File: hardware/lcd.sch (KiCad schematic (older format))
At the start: 3 parts, among them J6 LCD Display

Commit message: Hardware Projekt knovertiert von KiCad 4 -> KiCad 5 - Schaltplan angepasst - neues Detailfoto hinzugefügt - Footprints neu zugeordnet, somit ist auch wieder eine 3D Darstellung möglich - Readme.md angepasst
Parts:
- J6: footprint w_conn_strip:vasch_strip_5x2 -> Connector_IDC:IDC-Header_2x05_P2.54mm_Vertical; symbol Conn_02x05_Odd_Even -> Connector_Generic:Conn_02x05_Odd_Even
- R10: footprint Discret:R4-5 -> Resistor_THT:R_Axial_DIN0207_L6.3mm_D2.5mm_P10.16mm_Horizontal; symbol R -> Device:R
- RV1: footprint w_pth_resistors:trimmer_vishay_64w -> Potentiometer_THT:Potentiometer_Bourns_3296W_Vertical; symbol POT-RESCUE-1541-rebuild -> Device:R_POT
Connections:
- net labels added: D4, D5, D6, D7
- net labels removed: D0, D1, D2, D3
- wire segments 14 -> 16
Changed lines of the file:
@@
-EESchema Schematic File Version 2
-LIBS:power
-LIBS:1541-rebuild-rescue
-LIBS:device
-LIBS:transistors
-LIBS:conn
-LIBS:linear
-LIBS:regul
-LIBS:74xx
-LIBS:cmos4000
-LIBS:adc-dac
-LIBS:memory
-LIBS:xilinx
-LIBS:microcontrollers
-LIBS:dsp
-LIBS:microchip
-LIBS:analog_switches
-LIBS:motorola
-LIBS:texas
-LIBS:intel
-LIBS:audio
-LIBS:interface
-LIBS:digital-audio
-LIBS:philips
-LIBS:display
-LIBS:cypress
-LIBS:siliconi
-LIBS:opto
-LIBS:atmel
-LIBS:contrib
-LIBS:valves
-LIBS:Oscillators
-LIBS:w_analog
-LIBS:w_connectors
-LIBS:w_device
-LIBS:w_logic
-LIBS:w_memory
-LIBS:w_microcontrollers
-LIBS:w_opto
-LIBS:w_relay
-LIBS:w_rtx
-LIBS:w_transistor
-LIBS:w_vacuum
-LIBS:ka_sd_sockets
+EESchema Schematic File Version 4
 LIBS:1541-rebuild-cache
-EELAYER 25 0
+EELAYER 30 0
 EELAYER END
 $Descr A4 11693 8268
@@
 Sheet 3 4
 Title "1541-rebuid"
-Date "2018-05-16"
-Rev "1.3.5"
+Date "2020-04-14"
+Rev "1.4.0"
 Comp ""
 Comment1 "Erstellt von: Thorsten Kattanek"
@@
 $EndDescr
 $Comp
-L Conn_02x05_Odd_Even J6
+L Connector_Generic:Conn_02x05_Odd_Even J6
 U 1 1 5AEE2FA0
 P 5050 3600
 F 0 "J6" H 5100 3900 50  0000 C CNN
 F 1 "LCD Display" H 5100 3300 50  0000 C CNN
-F 2 "w_conn_strip:vasch_strip_5x2" H 5050 3600 50  0001 C CNN
+F 2 "Connector_IDC:IDC-Header_2x05_P2.54mm_Vertical" H 5050 3600 50  0001 C CNN
 F 3 "" H 5050 3600 50  0001 C CNN
 	1    5050 3600
@@
 Steckerbelegung für das LCD Display (20x4)\n\nPIN_01: VDD(2) ... +5V\nPIN_02: VSS(1), R/W(5), LED-/K(16) ... GND\nPIN_03: D4(11)\nPIN_04: D5(12)\nPIN_05: D6(13)\nPIN_06: D7(14)\nPIN_07: E(6)\nPIN_08: RS(4)\nPIN_09: LED+/A(15)\nPIN_10: VO(3)\n
 $Comp
-L +5V #PWR020
+L power:+5V #PWR0102
 U 1 1 5AEE3573
 P 5250 2450
-F 0 "#PWR020" H 5250 2300 50  0001 C CNN
+F 0 "#PWR0102" H 5250 2300 50  0001 C CNN
 F 1 "+5V" H 5250 2590 50  0000 C CNN
 F 2 "" H 5250 2450 60  0000 C CNN
@@
 $EndComp
 Text HLabel 5150 2900 1    60   Input ~ 0
-D0
+D4
 Text HLabel 5150 4150 3    60   Input ~ 0
-D1
+D5
 Text HLabel 5050 2900 1    60   Input ~ 0
-D2
+D6
 Text HLabel 5050 4150 3    60   Input ~ 0
-D3
+D7
 Text HLabel 4950 2900 1    60   Input ~ 0
 EN
@@
 RS
 Wire Wire Line
-	5250 2450 5250 3400
+	5250 2450 5250 2550
 Wire Wire Line
 	5150 2900 5150 3400
@@
 	4950 3900 4950 4150
 $Comp
-L R R10
+L Device:R R10
 U 1 1 5AEE40E3
 P 4850 3100
 F 0 "R10" V 4930 3100 50  0000 C CNN
 F 1 "150" V 4850 3100 50  0000 C CNN
-F 2 "Discret:R4-5" V 4780 3100 30  0001 C CNN
+F 2 "Resistor_THT:R_Axial_DIN0207_L6.3mm_D2.5mm_P10.16mm_Horizontal" V 4780 3100 30  0001 C CNN
 F 3 "" H 4850 3100 30  0000 C CNN
 	1    4850 3100
@@
 	4850 3250 4850 3400
 Wire Wire Line
-	5250 3900 5250 4750
+	5250 3900 5250 4550
 $Comp
-L POT-RESCUE-1541-rebuild RV1
+L Device:R_POT RV1
 U 1 1 5AEE481D
 P 4850 4550
-F 0 "RV1" H 4850 4450 50  0000 C CNN
-F 1 "10k" H 4850 4550 50  0000 C CNN
-F 2 "w_pth_resistors:trimmer_vishay_64w" H 4850 4550 60  0001 C CNN
+F 0 "RV1" V 4750 4550 50  0000 C CNN
+F 1 "10k" V 4850 4550 50  0000 C CNN
+F 2 "Potentiometer_THT:Potentiometer_Bourns_3296W_Vertical" H 4850 4550 60  0001 C CNN
 F 3 "" H 4850 4550 60  0000 C CNN
 	1    4850 4550
-	1    0    0    -1
+	0    -1   -1   0
 $EndComp
 Wire Wire Line
-	5100 4550 5250 4550
+	5000 4550 5250 4550
 Connection ~ 5250 4550
 Wire Wire Line
 	4850 3900 4850 4400
 $Comp
-L +5V #PWR021
+L power:+5V #PWR0103
 U 1 1 5AEE4960
 P 4350 4550
-F 0 "#PWR021" H 4350 4400 50  0001 C CNN
+F 0 "#PWR0103" H 4350 4400 50  0001 C CNN
 F 1 "+5V" H 4350 4690 50  0000 C CNN
 F 2 "" H 4350 4550 60  0000 C CNN
@@
 $EndComp
 Wire Wire Line
-	4350 4550 4600 4550
+	4350 4550 4700 4550
 Text Notes 650  7600 0    60   ~ 0
 R10 hängt von der Hintergrundbeleuchtung des LCD Displays ab !
 $Comp
-L GND #PWR022
+L power:GND #PWR0104
 U 1 1 5AF0CC1F
 P 5250 4750
-F 0 "#PWR022" H 5250 4500 50  0001 C CNN
+F 0 "#PWR0104" H 5250 4500 50  0001 C CNN
 F 1 "GND" H 5250 4600 50  0000 C CNN
 F 2 "" H 5250 4750 50  0001 C CNN
@@
 	1    0    0    -1
 $EndComp
+Wire Wire Line
+	5250 2550 5250 3400
+Wire Wire Line
+	5250 4550 5250 4750
 $EndSCHEMATC

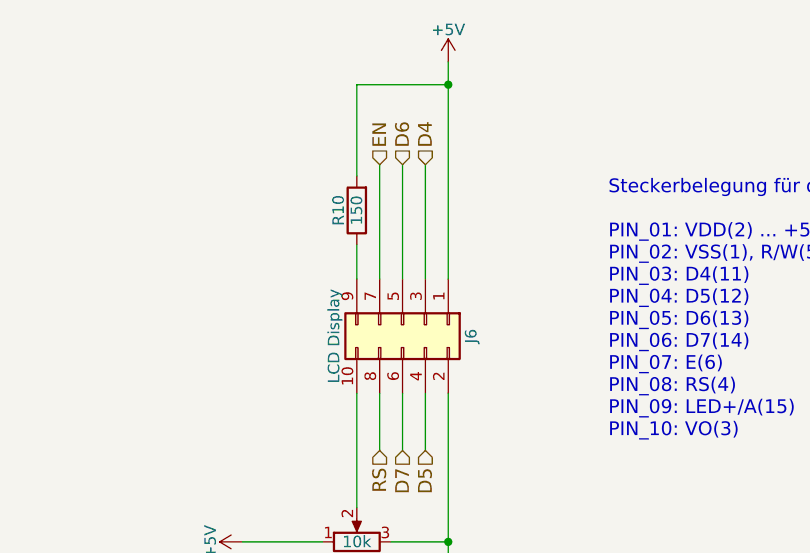
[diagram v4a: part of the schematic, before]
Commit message: Platine geändert - größe angepasst für 1541 I + II - Bauteile neu angeordnet - Beschriftungen hinzugefügt
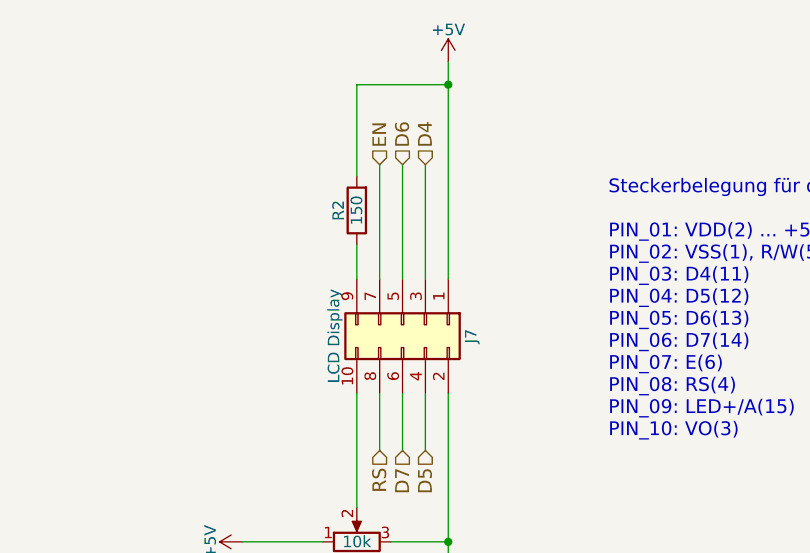
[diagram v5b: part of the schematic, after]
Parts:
- renumbered J6 to J7, R10 to R2
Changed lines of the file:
@@
 $EndDescr
 $Comp
-L Connector_Generic:Conn_02x05_Odd_Even J6
+L Connector_Generic:Conn_02x05_Odd_Even J7
 U 1 1 5AEE2FA0
 P 5050 3600
-F 0 "J6" H 5100 3900 50  0000 C CNN
+F 0 "J7" H 5100 3900 50  0000 C CNN
 F 1 "LCD Display" H 5100 3300 50  0000 C CNN
 F 2 "Connector_IDC:IDC-Header_2x05_P2.54mm_Vertical" H 5050 3600 50  0001 C CNN
@@
 Steckerbelegung für das LCD Display (20x4)\n\nPIN_01: VDD(2) ... +5V\nPIN_02: VSS(1), R/W(5), LED-/K(16) ... GND\nPIN_03: D4(11)\nPIN_04: D5(12)\nPIN_05: D6(13)\nPIN_06: D7(14)\nPIN_07: E(6)\nPIN_08: RS(4)\nPIN_09: LED+/A(15)\nPIN_10: VO(3)\n
 $Comp
-L power:+5V #PWR0102
+L power:+5V #PWR021
 U 1 1 5AEE3573
 P 5250 2450
-F 0 "#PWR0102" H 5250 2300 50  0001 C CNN
+F 0 "#PWR021" H 5250 2300 50  0001 C CNN
 F 1 "+5V" H 5250 2590 50  0000 C CNN
 F 2 "" H 5250 2450 60  0000 C CNN
@@
 	4950 3900 4950 4150
 $Comp
-L Device:R R10
+L Device:R R2
 U 1 1 5AEE40E3
 P 4850 3100
-F 0 "R10" V 4930 3100 50  0000 C CNN
+F 0 "R2" V 4930 3100 50  0000 C CNN
 F 1 "150" V 4850 3100 50  0000 C CNN
 F 2 "Resistor_THT:R_Axial_DIN0207_L6.3mm_D2.5mm_P10.16mm_Horizontal" V 4780 3100 30  0001 C CNN
@@
 	4850 3900 4850 4400
 $Comp
-L power:+5V #PWR0103
+L power:+5V #PWR022
 U 1 1 5AEE4960
 P 4350 4550
-F 0 "#PWR0103" H 4350 4400 50  0001 C CNN
+F 0 "#PWR022" H 4350 4400 50  0001 C CNN
 F 1 "+5V" H 4350 4690 50  0000 C CNN
 F 2 "" H 4350 4550 60  0000 C CNN
@@
 R10 hängt von der Hintergrundbeleuchtung des LCD Displays ab !
 $Comp
-L power:GND #PWR0104
+L power:GND #PWR023
 U 1 1 5AF0CC1F
 P 5250 4750
-F 0 "#PWR0104" H 5250 4500 50  0001 C CNN
+F 0 "#PWR023" H 5250 4500 50  0001 C CNN
 F 1 "GND" H 5250 4600 50  0000 C CNN
 F 2 "" H 5250 4750 50  0001 C CNN

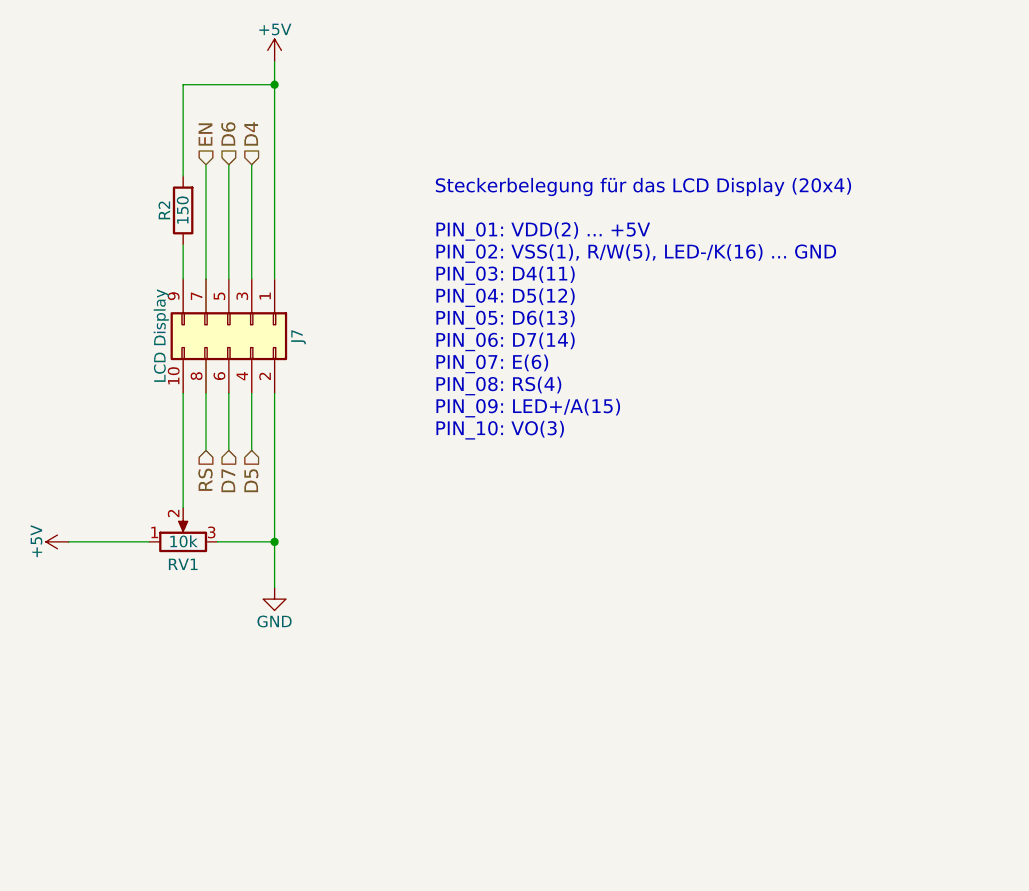
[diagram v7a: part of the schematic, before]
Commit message: major changes for 1.4.1 PCB
created a new PCB for I2C support. all connections rerouted and
a new board needs to be created. layout and footprint taken from 1.4.0
board revision. images from kicad added, README adopted
CAUTION: PCB untested, due to lack of software routines (I2C)
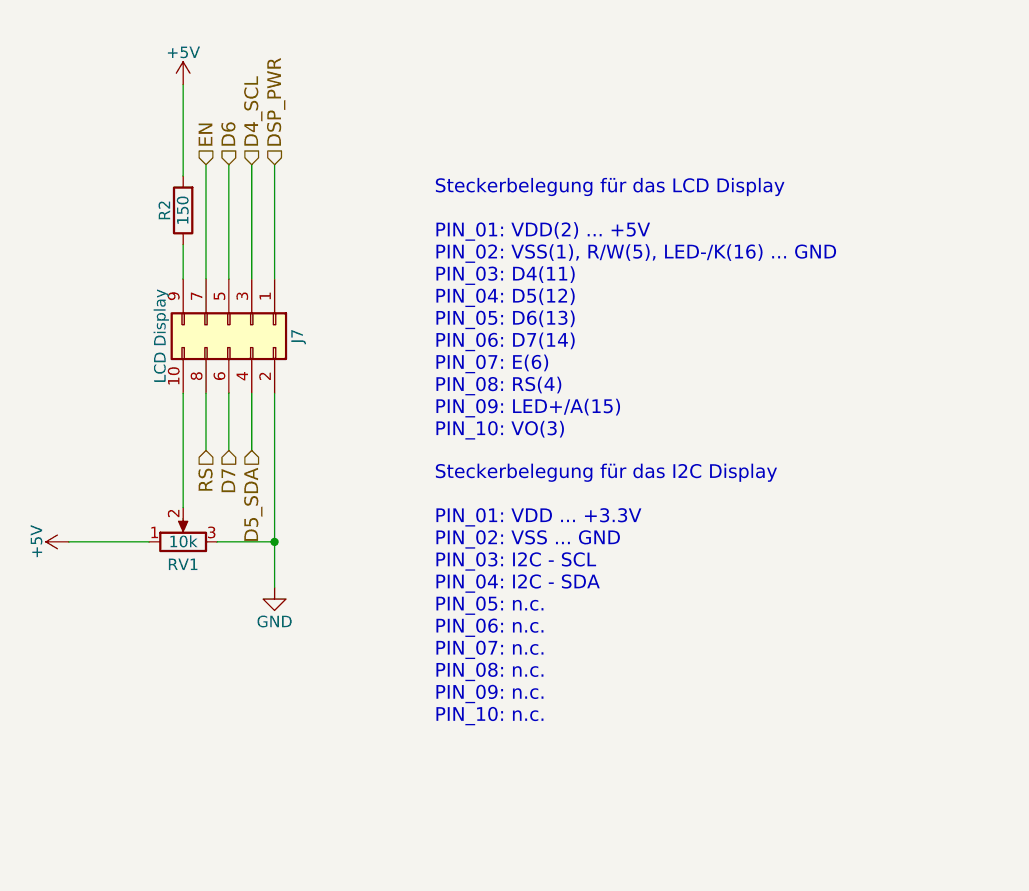
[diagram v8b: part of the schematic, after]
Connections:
- net +5V: no longer J7.1 (Pin_1)
- net D4 renamed D4_SCL
- net D5 renamed D5_SDA
- new net DSP_PWR: J7.1 (Pin_1)
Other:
- note added: "Steckerbelegung für das I2C Display\n\nPIN_01: VDD ... +3.3V\nPIN_02: VSS ... GND\nPIN_03: I2C - SCL\nPIN_04: I2C - SDA\nPIN_05: n.c.\nPIN_06: n.c.\nPIN_07: n.c.\nPIN_08: n.c.\nPIN_09: n.c.\nPIN_10: n.c.\n"
- note added: "Steckerbelegung für das LCD Display\n\nPIN_01: VDD(2) ... +5V\nPIN_02: VSS(1), R/W(5), LED-/K(16) ... GND\nPIN_03: D4(11)\nPIN_04: D5(12)\nPIN_05: D6(13)\nPIN_06: D7(14)\nPIN_07: E(6)\nPIN_08: RS(4)\nPIN_09: LED+/A(15)\nPIN_10: VO(3)\n"
- note removed: "Steckerbelegung für das LCD Display (20x4)\n\nPIN_01: VDD(2) ... +5V\nPIN_02: VSS(1), R/W(5), LED-/K(16) ... GND\nPIN_03: D4(11)\nPIN_04: D5(12)\nPIN_05: D6(13)\nPIN_06: D7(14)\nPIN_07: E(6)\nPIN_08: RS(4)\nPIN_09: LED+/A(15)\nPIN_10: VO(3)\n"
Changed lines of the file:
@@
 EESchema Schematic File Version 4
-LIBS:1541-rebuild-cache
 EELAYER 30 0
 EELAYER END
@@
 Sheet 2 3
 Title "1541-rebuid"
-Date "2020-04-18"
-Rev "1.4.0"
+Date "2021-08-23"
+Rev "1.4.1"
 Comp ""
 Comment1 "Erstellt von: Thorsten Kattanek"
-Comment2 ""
+Comment2 "redesign and i2c added: F00K42"
 Comment3 ""
 Comment4 ""
@@
 $EndComp
 Text Notes 5950 4100 0    60   ~ 0
-Steckerbelegung für das LCD Display (20x4)\n\nPIN_01: VDD(2) ... +5V\nPIN_02: VSS(1), R/W(5), LED-/K(16) ... GND\nPIN_03: D4(11)\nPIN_04: D5(12)\nPIN_05: D6(13)\nPIN_06: D7(14)\nPIN_07: E(6)\nPIN_08: RS(4)\nPIN_09: LED+/A(15)\nPIN_10: VO(3)\n
-$Comp
-L power:+5V #PWR021
-U 1 1 5AEE3573
-P 5250 2450
-F 0 "#PWR021" H 5250 2300 50  0001 C CNN
-F 1 "+5V" H 5250 2590 50  0000 C CNN
-F 2 "" H 5250 2450 60  0000 C CNN
-F 3 "" H 5250 2450 60  0000 C CNN
-	1    5250 2450
-	1    0    0    -1
-$EndComp
+Steckerbelegung für das LCD Display\n\nPIN_01: VDD(2) ... +5V\nPIN_02: VSS(1), R/W(5), LED-/K(16) ... GND\nPIN_03: D4(11)\nPIN_04: D5(12)\nPIN_05: D6(13)\nPIN_06: D7(14)\nPIN_07: E(6)\nPIN_08: RS(4)\nPIN_09: LED+/A(15)\nPIN_10: VO(3)\n
 Text HLabel 5150 2900 1    60   Input ~ 0
-D4
+D4_SCL
 Text HLabel 5150 4150 3    60   Input ~ 0
-D5
+D5_SDA
 Text HLabel 5050 2900 1    60   Input ~ 0
 D6
@@
 Text HLabel 4950 4150 3    60   Input ~ 0
 RS
-Wire Wire Line
-	5250 2450 5250 2550
 Wire Wire Line
 	5150 2900 5150 3400
@@
 Wire Wire Line
 	4850 2950 4850 2550
-Wire Wire Line
-	4850 2550 5250 2550
-Connection ~ 5250 2550
 Wire Wire Line
 	4850 3250 4850 3400
@@
 $EndComp
 Wire Wire Line
-	5250 2550 5250 3400
+	5250 4550 5250 4750
+$Comp
+L power:+5V #PWR0106
+U 1 1 615307BF
+P 4850 2550
+F 0 "#PWR0106" H 4850 2400 50  0001 C CNN
+F 1 "+5V" H 4850 2690 50  0000 C CNN
+F 2 "" H 4850 2550 60  0000 C CNN
+F 3 "" H 4850 2550 60  0000 C CNN
+	1    4850 2550
+	1    0    0    -1
+$EndComp
+Text HLabel 5250 2900 1    60   Input ~ 0
+DSP_PWR
 Wire Wire Line
-	5250 4550 5250 4750
+	5250 3400 5250 2900
+Text Notes 5950 5350 0    60   ~ 0
+Steckerbelegung für das I2C Display\n\nPIN_01: VDD ... +3.3V\nPIN_02: VSS ... GND\nPIN_03: I2C - SCL\nPIN_04: I2C - SDA\nPIN_05: n.c.\nPIN_06: n.c.\nPIN_07: n.c.\nPIN_08: n.c.\nPIN_09: n.c.\nPIN_10: n.c.\n
 $EndSCHEMATC
